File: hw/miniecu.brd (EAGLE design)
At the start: 50 x 50 mm, 63 parts

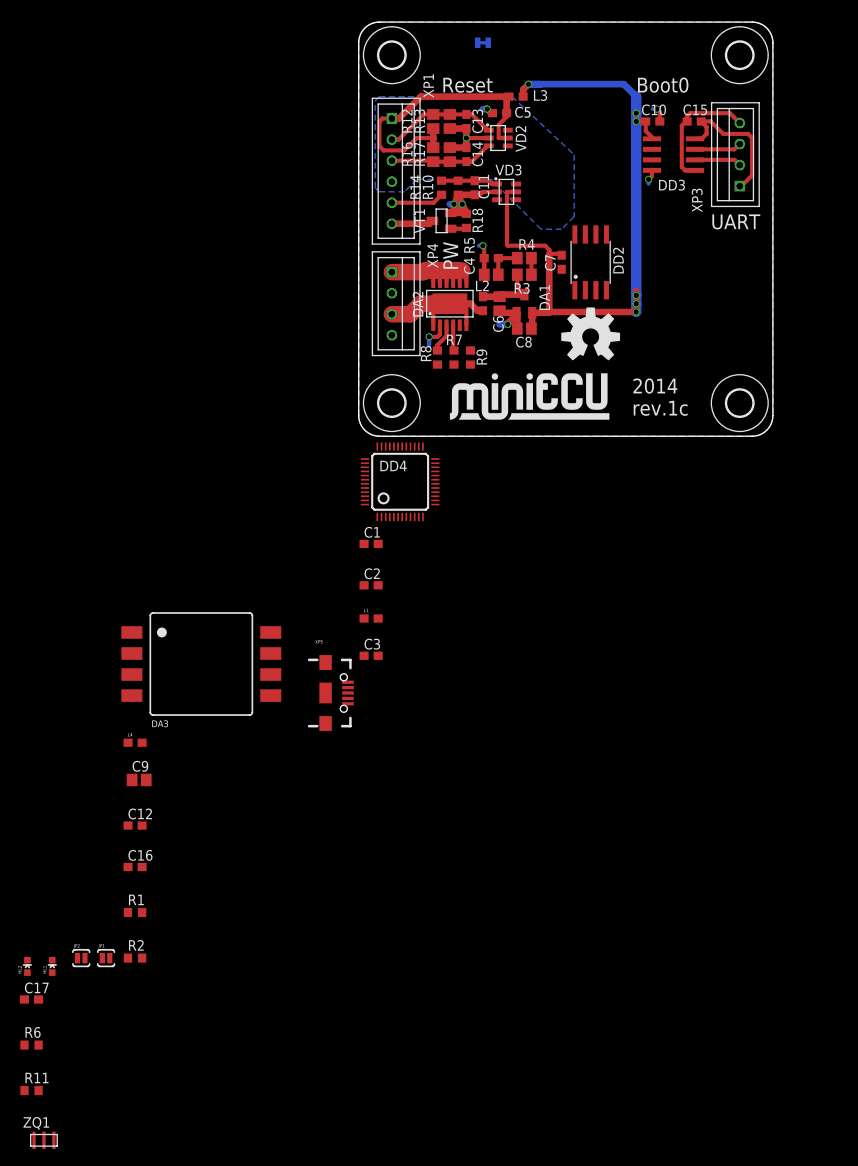
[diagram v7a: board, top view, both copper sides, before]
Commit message: hw: do half connections of v2
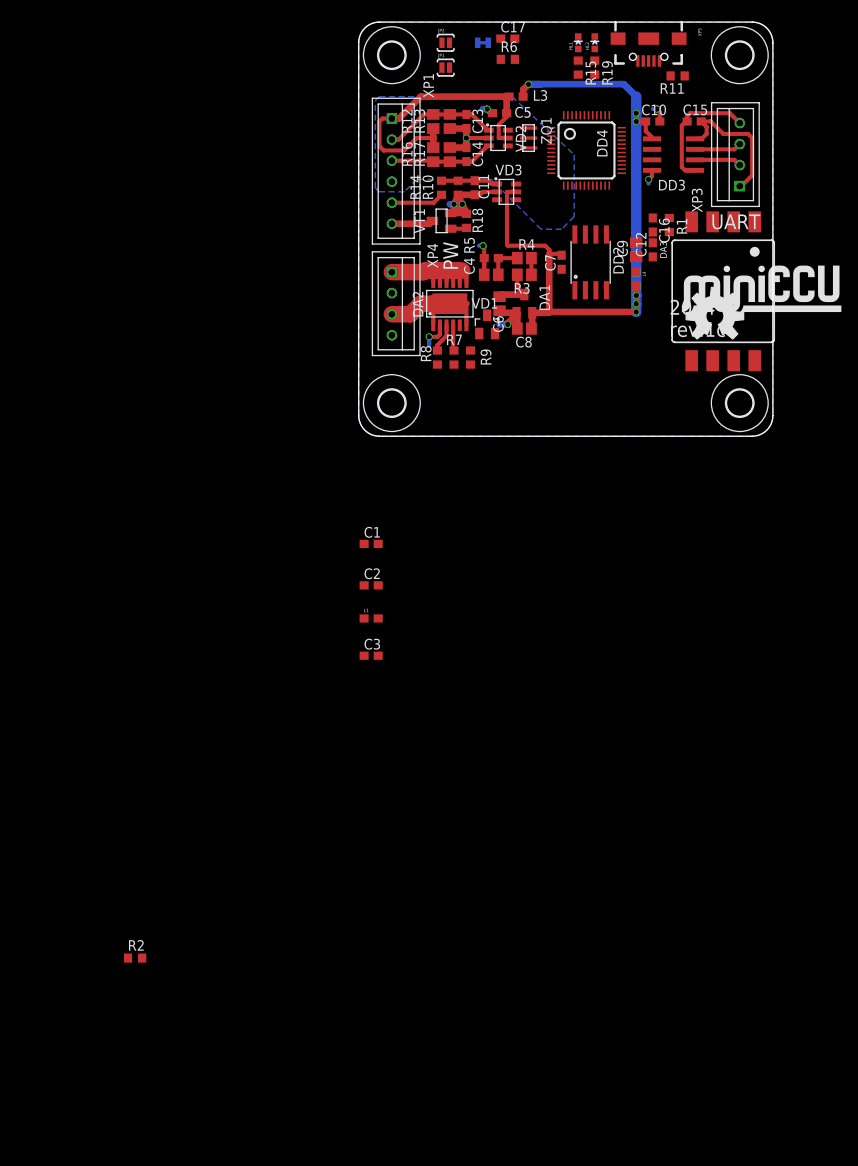
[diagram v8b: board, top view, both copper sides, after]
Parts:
- removed L2: FB, SparkFun-Passives:0603
- added R15, R19: 140, resistor:R0603
- added VD1: BAT54C, diode:SOT23
- moved R11 145.2 mm to (38.5, 43.5), turned to 180 degrees
- moved ZQ1 134.4 mm to (20.5, 36.0), turned to 270 degrees
- moved R6 132.2 mm to (18.0, 45.5)
- moved HL2 130.9 mm to (28.5, 47.5)
- moved C17 129.5 mm to (18.0, 48.0)
- moved HL1 128.3 mm to (26.5, 47.5)
- moved JP2 118.9 mm to (10.5, 47.5)
- moved JP1 115.1 mm to (10.5, 44.5)
- moved R1 105.1 mm to (37.5, 25.5), turned to 270 degrees
- moved C16 99.6 mm to (35.5, 25.5), turned to 270 degrees
- moved C12 93.5 mm to (35.5, 22.5), turned to 90 degrees
- moved XP5 88.1 mm to (35.0, 48.0), turned to 270 degrees
- moved C9 87.7 mm to (33.5, 22.5), turned to 90 degrees
- moved L4 82.4 mm to (33.5, 19.0), turned to 270 degrees
- moved DA3 77.4 mm to (44.0, 17.5), turned to 270 degrees
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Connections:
- new net LED_G: R15.2
- new net LED_R: R19.2
- new net N$12: HL2.A, R19.1
- new net N$8: HL1.A, R15.1
- new net OSC32I: DD4.3
- new net OSC32O: DD4.4
- new net SWCLK: DD4.37
- new net SWDIO: DD4.34
- net +3V3: now also R11.2
- net FLOW: now also DD4.21
- net GND: now also HL1.C, HL2.C
- net N$6: now also VD1.3; no longer L2.1
- net OIL_PRES: now also DD4.19
- net RPM_IN: now also DD4.10
- net RXD: now also DD4.31
- net THERM: now also DD4.18
- net TXD: now also DD4.30
- net USB_DM: now also DD4.32
- net USB_DP: now also DD4.33, R11.1
- net USB_VBUS: now also VD1.2
- net VBAT: now also VD1.1; no longer L2.2
- net V_SENSE: now also DD4.20
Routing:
- net VBAT: track 17.1 -> 14.7 mm
- net N$6: track 7.86 -> 5.86 mm
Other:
- board text removed: "Boot0"
- board text removed: "Reset"
